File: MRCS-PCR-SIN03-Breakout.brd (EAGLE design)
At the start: 99.8 x 68.8 mm, 10 parts

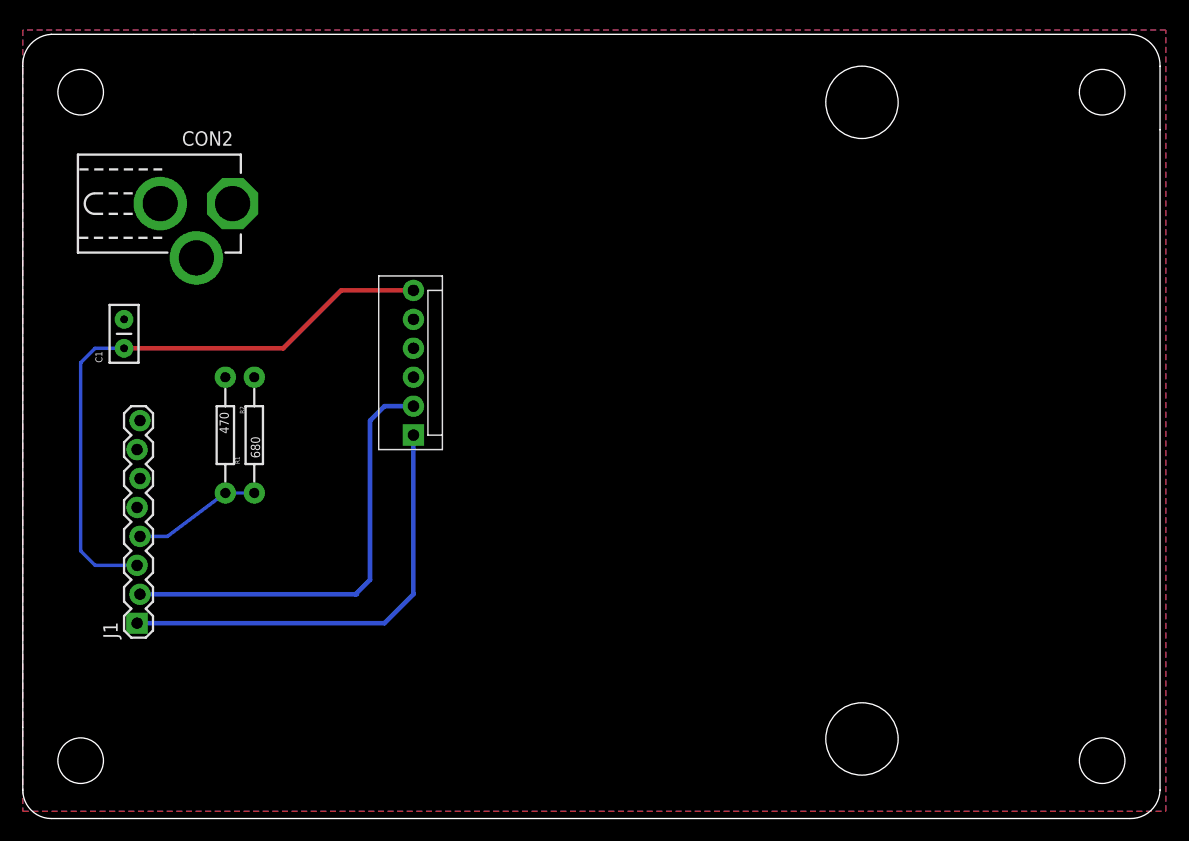
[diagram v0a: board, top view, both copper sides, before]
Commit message: Added 8 mm screw barrier block
this might be more useful for the phone folks as it supports spade lugs. Plenty of room on the board!
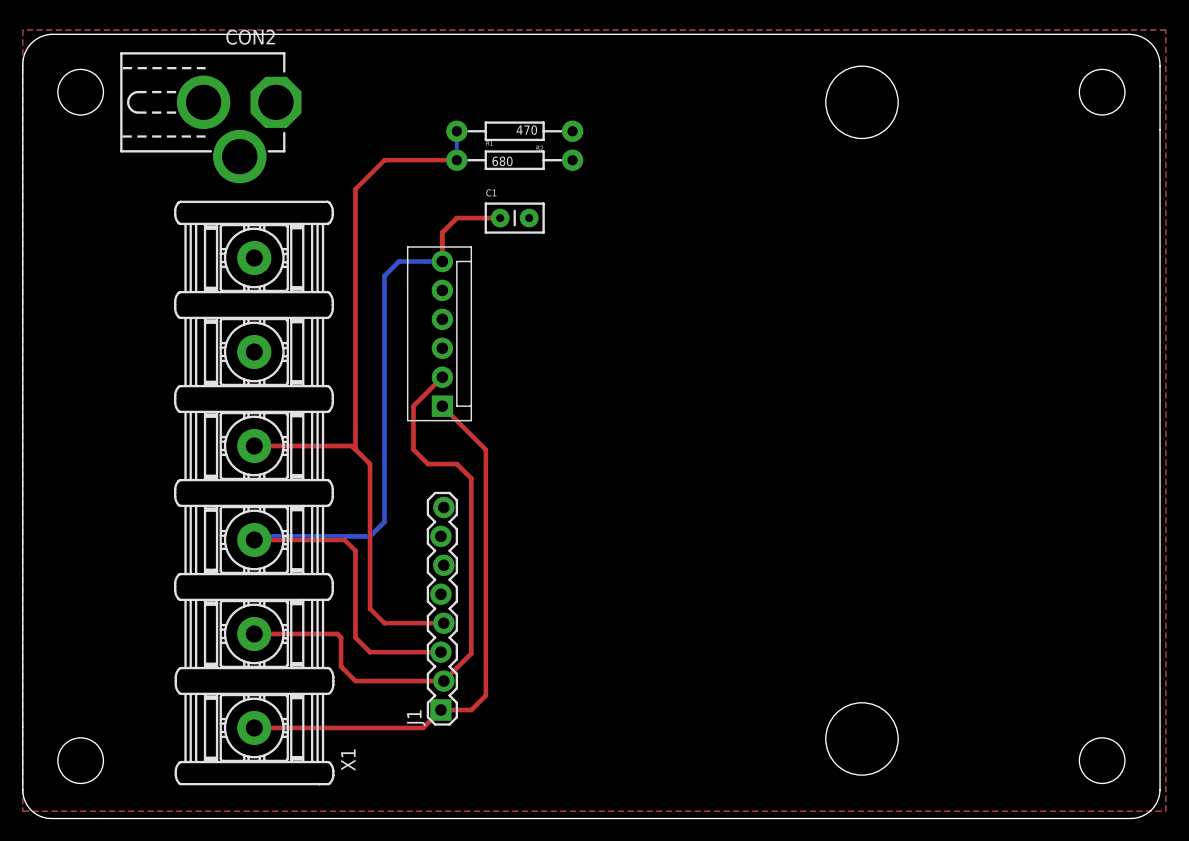
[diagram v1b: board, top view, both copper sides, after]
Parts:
- added X1: 5202-06-N-02, con-ebyelectro:5202-06-N-02
- moved R2 36.8 mm to (43.2, 61.0), turned to 180 degrees
- moved C1 35.8 mm to (43.2, 53.3), turned to 0 degrees
- moved R1 33.2 mm to (43.2, 58.4), turned to 0 degrees
- moved J1 27.7 mm to (36.8, 10.2)
- moved U$3 23.7 mm to (66.0, 54.6)
- moved CON2 9.67 mm to (19.1, 63.5)
- moved U$4 8.03 mm to (64.8, 36.8)
- moved U$2 4.02 mm to (48.3, 8.89)
- moved CON3 3.59 mm to (36.8, 36.8)
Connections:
- net 5VR: now also X1.4
- net GND: now also CON3.4, X1.5
- net INH: now also X1.3
- net O1: now also X1.1
- net O2: now also X1.2
- net VCC: now also X1.6
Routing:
- net 5VR: track 11.3 -> 65.9 mm
- net INH: track 53.8 -> 72.4 mm
- net O2: track 39.2 -> 52.2 mm
- net O1: track 39.3 -> 48.5 mm
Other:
- board text added: "V G R I O O"
- board text added: "Version 1.2 20231007"
- board text removed: "Version 1.1 20231002"
